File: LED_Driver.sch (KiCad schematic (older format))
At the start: 6 parts

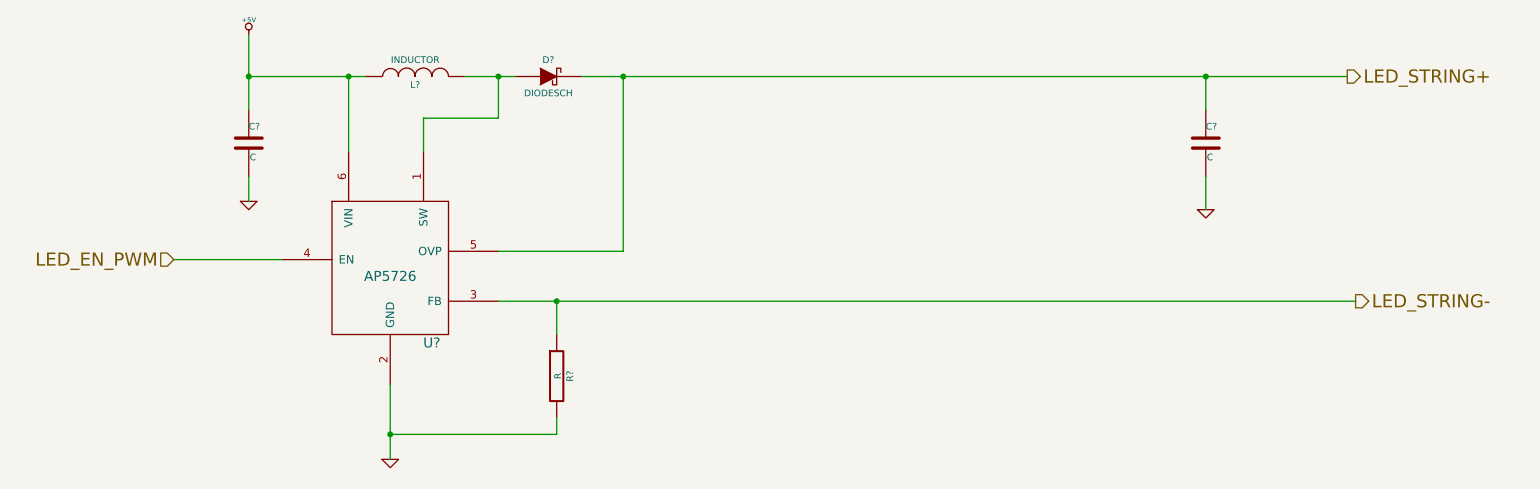
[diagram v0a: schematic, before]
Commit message: Added Relay module footprints.
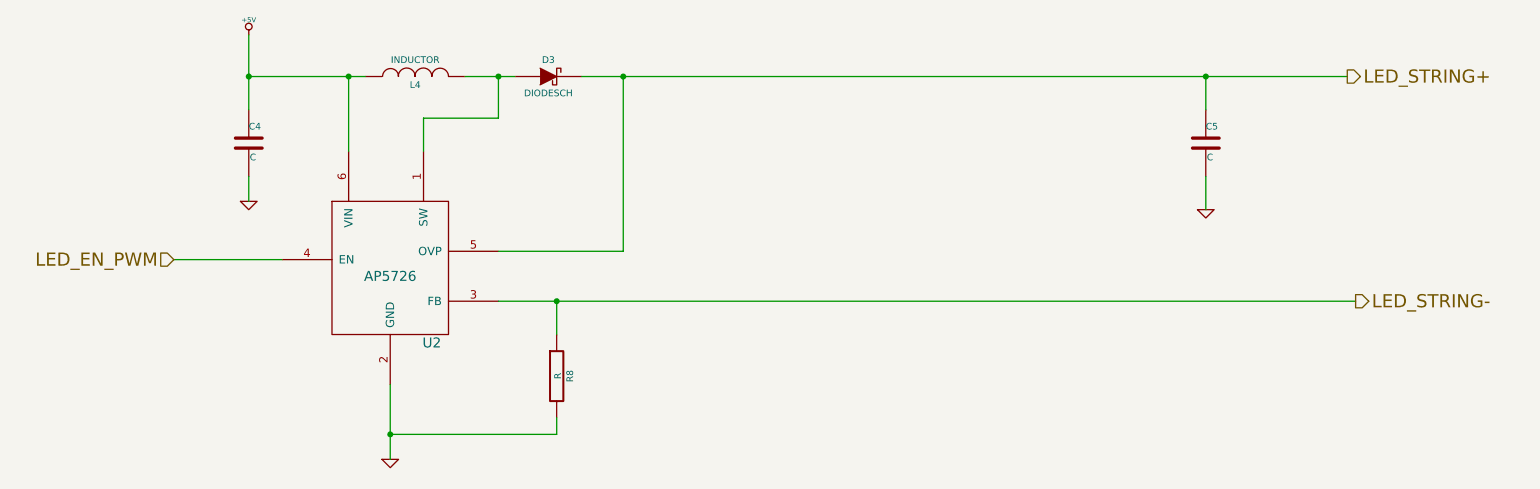
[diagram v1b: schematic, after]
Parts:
- gave numbers to parts that had none: 6
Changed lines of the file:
@@
 LIBS:valves
 LIBS:BB
+LIBS:GLSP
 LIBS:BB-cache
 EELAYER 24 0
@@
 $Descr A4 11693 8268
 encoding utf-8
-Sheet 6 9
+Sheet 4 9
 Title ""
 Date ""
@@
 LED_STRING-
 $Comp
-L AP5726 U?
+L AP5726 U2
 U 1 1 52F7C670
 P 2900 2600
-F 0 "U?" H 3150 2100 60  0000 C CNN
+F 0 "U2" H 3150 2100 60  0000 C CNN
 F 1 "AP5726" H 2900 2500 60  0000 C CNN
 F 2 "" H 2900 2650 60  0000 C CNN
@@
 	1600 2600 2250 2600
 $Comp
-L +5V #PWR?
+L +5V #PWR20
 U 1 1 52F7C764
 P 2050 1250
-F 0 "#PWR?" H 2050 1340 20  0001 C CNN
+F 0 "#PWR20" H 2050 1340 20  0001 C CNN
 F 1 "+5V" H 2050 1340 30  0000 C CNN
 F 2 "" H 2050 1250 60  0000 C CNN
@@
 $EndComp
 $Comp
-L GND #PWR?
+L GND #PWR21
 U 1 1 52F7C778
 P 2050 2250
-F 0 "#PWR?" H 2050 2250 30  0001 C CNN
+F 0 "#PWR21" H 2050 2250 30  0001 C CNN
 F 1 "GND" H 2050 2180 30  0001 C CNN
 F 2 "" H 2050 2250 60  0000 C CNN
@@
 $EndComp
 $Comp
-L C C?
+L C C4
 U 1 1 52F7C794
 P 2050 1900
-F 0 "C?" H 2050 2000 40  0000 L CNN
+F 0 "C4" H 2050 2000 40  0000 L CNN
 F 1 "C" H 2056 1815 40  0000 L CNN
 F 2 "" H 2088 1750 30  0000 C CNN
@@
 Connection ~ 2050 1500
 $Comp
-L INDUCTOR L?
+L INDUCTOR L4
 U 1 1 52F7C7DA
 P 3050 1500
-F 0 "L?" V 3000 1500 40  0000 C CNN
+F 0 "L4" V 3000 1500 40  0000 C CNN
 F 1 "INDUCTOR" V 3150 1500 40  0000 C CNN
 F 2 "" H 3050 1500 60  0000 C CNN
@@
 	3100 1750 3100 1950
 $Comp
-L C C?
+L C C5
 U 1 1 52F7C800
 P 7800 1900
-F 0 "C?" H 7800 2000 40  0000 L CNN
+F 0 "C5" H 7800 2000 40  0000 L CNN
 F 1 "C" H 7806 1815 40  0000 L CNN
 F 2 "" H 7838 1750 30  0000 C CNN
@@
 $EndComp
 $Comp
-L DIODESCH D?
+L DIODESCH D3
 U 1 1 52F7C80D
 P 3850 1500
-F 0 "D?" H 3850 1600 40  0000 C CNN
+F 0 "D3" H 3850 1600 40  0000 C CNN
 F 1 "DIODESCH" H 3850 1400 40  0000 C CNN
 F 2 "" H 3850 1500 60  0000 C CNN
@@
 Connection ~ 7800 1500
 $Comp
-L GND #PWR?
+L GND #PWR23
 U 1 1 52F7C993
 P 7800 2300
-F 0 "#PWR?" H 7800 2300 30  0001 C CNN
+F 0 "#PWR23" H 7800 2300 30  0001 C CNN
 F 1 "GND" H 7800 2230 30  0001 C CNN
 F 2 "" H 7800 2300 60  0000 C CNN
@@
 	3550 2850 8700 2850
 $Comp
-L R R?
+L R R8
 U 1 1 52F7CA2A
 P 3900 3300
-F 0 "R?" V 3980 3300 40  0000 C CNN
+F 0 "R8" V 3980 3300 40  0000 C CNN
 F 1 "R" V 3907 3301 40  0000 C CNN
 F 2 "" V 3830 3300 30  0000 C CNN
@@
 $EndComp
 $Comp
-L GND #PWR?
+L GND #PWR22
 U 1 1 52F7CA46
 P 2900 3800
-F 0 "#PWR?" H 2900 3800 30  0001 C CNN
+F 0 "#PWR22" H 2900 3800 30  0001 C CNN
 F 1 "GND" H 2900 3730 30  0001 C CNN
 F 2 "" H 2900 3800 60  0000 C CNN

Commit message: Layout sessions 1-4.
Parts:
- C4, C5: value C -> 1u
- D3: value DIODESCH -> B0540WS-7; MFG Part Number (none) -> B0540WS-7
- L4: value INDUCTOR -> 22u; MFG Part Number (none) -> NR4012T220M; MFG name (none) -> Taiyo Yuden
- R8: value R -> 15
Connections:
- net +5V renamed +5P
- net GND renamed GND_LED
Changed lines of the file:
@@
 $Descr A4 11693 8268
 encoding utf-8
-Sheet 4 9
+Sheet 7 9
 Title ""
 Date ""
@@
 	1600 2600 2250 2600
 $Comp
-L +5V #PWR052
-U 1 1 52F7C764
-P 2050 1250
-F 0 "#PWR052" H 2050 1340 20  0001 C CNN
-F 1 "+5V" H 2050 1340 30  0000 C CNN
-F 2 "" H 2050 1250 60  0000 C CNN
-F 3 "" H 2050 1250 60  0000 C CNN
-	1    2050 1250
-	1    0    0    -1
-$EndComp
-$Comp
-L GND #PWR053
-U 1 1 52F7C778
-P 2050 2250
-F 0 "#PWR053" H 2050 2250 30  0001 C CNN
-F 1 "GND" H 2050 2180 30  0001 C CNN
-F 2 "" H 2050 2250 60  0000 C CNN
-F 3 "" H 2050 2250 60  0000 C CNN
-	1    2050 2250
-	1    0    0    -1
-$EndComp
-$Comp
 L C C4
 U 1 1 52F7C794
 P 2050 1900
 F 0 "C4" H 2050 2000 40  0000 L CNN
-F 1 "C" H 2056 1815 40  0000 L CNN
+F 1 "1u" H 2056 1815 40  0000 L CNN
 F 2 "" H 2088 1750 30  0000 C CNN
 F 3 "" H 2050 1900 60  0000 C CNN
@@
 	1    0    0    -1
 $EndComp
-Wire Wire Line
-	2050 2100 2050 2250
 Wire Wire Line
 	2050 1250 2050 1700
@@
 P 3050 1500
 F 0 "L4" V 3000 1500 40  0000 C CNN
-F 1 "INDUCTOR" V 3150 1500 40  0000 C CNN
+F 1 "22u" V 3150 1500 40  0000 C CNN
 F 2 "" H 3050 1500 60  0000 C CNN
 F 3 "" H 3050 1500 60  0000 C CNN
+F 4 "Taiyo Yuden" H 3050 1500 60  0001 C CNN "MFG name"
+F 5 "NR4012T220M" H 3050 1500 60  0001 C CNN "MFG Part Number"
 	1    3050 1500
 	0    -1   -1   0
@@
 P 7800 1900
 F 0 "C5" H 7800 2000 40  0000 L CNN
-F 1 "C" H 7806 1815 40  0000 L CNN
+F 1 "1u" H 7806 1815 40  0000 L CNN
 F 2 "" H 7838 1750 30  0000 C CNN
 F 3 "" H 7800 1900 60  0000 C CNN
@@
 P 3850 1500
 F 0 "D3" H 3850 1600 40  0000 C CNN
-F 1 "DIODESCH" H 3850 1400 40  0000 C CNN
+F 1 "B0540WS-7" H 3850 1400 40  0000 C CNN
 F 2 "" H 3850 1500 60  0000 C CNN
 F 3 "" H 3850 1500 60  0000 C CNN
+F 4 "B0540WS-7" H 3850 1500 60  0001 C CNN "MFG Part Number"
 	1    3850 1500
 	1    0    0    -1
@@
 	7800 1500 7800 1700
 Connection ~ 7800 1500
-$Comp
-L GND #PWR054
-U 1 1 52F7C993
-P 7800 2300
-F 0 "#PWR054" H 7800 2300 30  0001 C CNN
-F 1 "GND" H 7800 2230 30  0001 C CNN
-F 2 "" H 7800 2300 60  0000 C CNN
-F 3 "" H 7800 2300 60  0000 C CNN
-	1    7800 2300
-	1    0    0    -1
-$EndComp
-Wire Wire Line
-	7800 2100 7800 2300
 Wire Wire Line
 	3550 2850 8700 2850
@@
 P 3900 3300
 F 0 "R8" V 3980 3300 40  0000 C CNN
-F 1 "R" V 3907 3301 40  0000 C CNN
+F 1 "15" V 3907 3301 40  0000 C CNN
 F 2 "" V 3830 3300 30  0000 C CNN
 F 3 "" H 3900 3300 30  0000 C CNN
 	1    3900 3300
-	1    0    0    -1
-$EndComp
-$Comp
-L GND #PWR055
-U 1 1 52F7CA46
-P 2900 3800
-F 0 "#PWR055" H 2900 3800 30  0001 C CNN
-F 1 "GND" H 2900 3730 30  0001 C CNN
-F 2 "" H 2900 3800 60  0000 C CNN
-F 3 "" H 2900 3800 60  0000 C CNN
-	1    2900 3800
 	1    0    0    -1
 $EndComp
@@
 	4300 2550 4300 1500
 Connection ~ 4300 1500
+$Comp
+L +5P #PWR53
+U 1 1 531356A8
+P 2050 1250
+F 0 "#PWR53" H 2050 1380 20  0001 C CNN
+F 1 "+5P" H 2050 1350 30  0000 C CNN
+F 2 "" H 2050 1250 60  0000 C CNN
+F 3 "" H 2050 1250 60  0000 C CNN
+	1    2050 1250
+	1    0    0    -1
+$EndComp
+$Comp
+L GND_LED #PWR044
+U 1 1 5313B578
+P 7800 2300
+F 0 "#PWR044" H 7800 2300 30  0001 C CNN
+F 1 "GND_LED" H 7800 2200 30  0000 C CNN
+F 2 "" H 7800 2300 60  0000 C CNN
+F 3 "" H 7800 2300 60  0000 C CNN
+	1    7800 2300
+	1    0    0    -1
+$EndComp
+Wire Wire Line
+	7800 2300 7800 2100
+Wire Wire Line
+	2050 2250 2050 2100
+$Comp
+L GND_LED #PWR045
+U 1 1 5313D53D
+P 2900 3800
+F 0 "#PWR045" H 2900 3800 30  0001 C CNN
+F 1 "GND_LED" H 2900 3730 30  0000 C CNN
+F 2 "" H 2900 3800 60  0000 C CNN
+F 3 "" H 2900 3800 60  0000 C CNN
+	1    2900 3800
+	1    0    0    -1
+$EndComp
+$Comp
+L GND_LED #PWR046
+U 1 1 5313D551
+P 2050 2250
+F 0 "#PWR046" H 2050 2250 30  0001 C CNN
+F 1 "GND_LED" H 2050 2180 30  0000 C CNN
+F 2 "" H 2050 2250 60  0000 C CNN
+F 3 "" H 2050 2250 60  0000 C CNN
+	1    2050 2250
+	1    0    0    -1
+$EndComp
 $EndSCHEMATC
